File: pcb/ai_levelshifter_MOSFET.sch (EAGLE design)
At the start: 15 parts, among them J1 1X06, J2 1X06NOFIRST, Q1 BSS138, Q2 BSS138, Q3 BSS138, Q4 BSS138

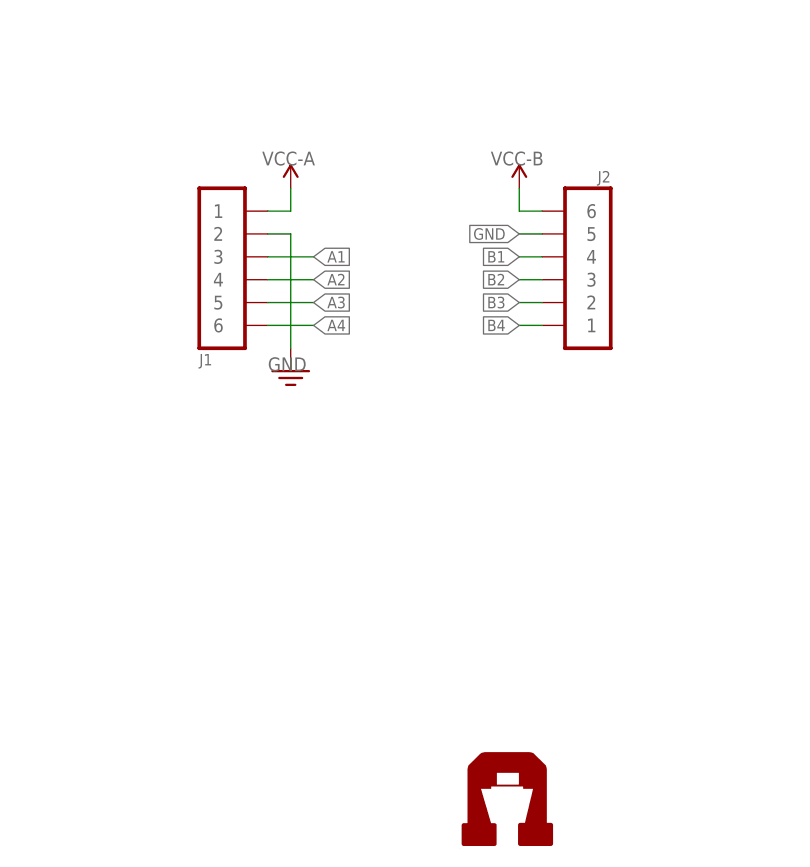
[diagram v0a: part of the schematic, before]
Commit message: fixed spacing to fit properly on a breadboard
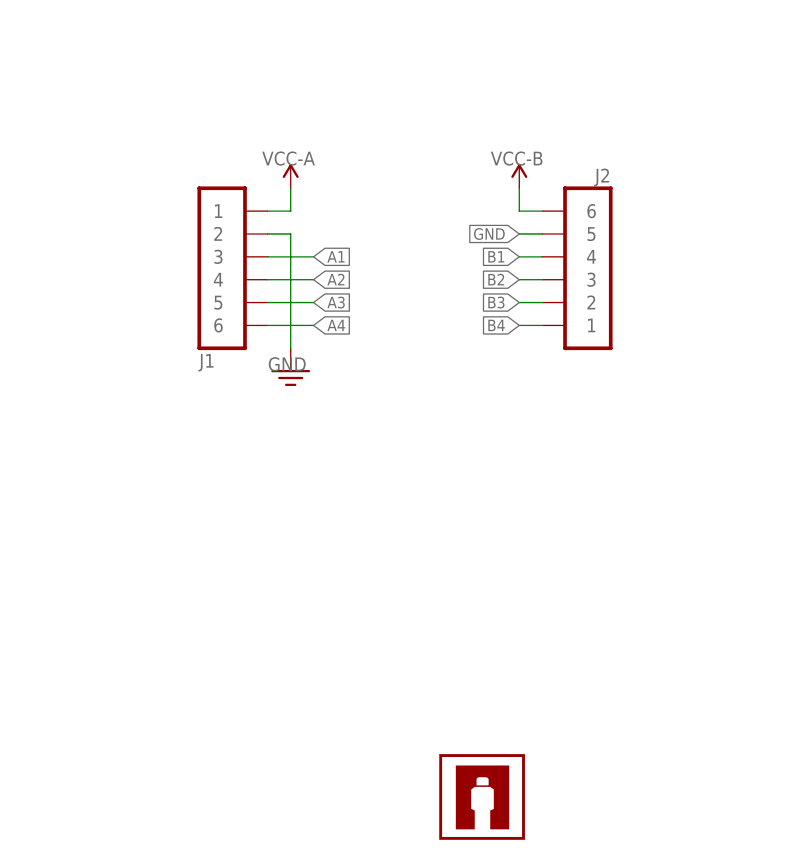
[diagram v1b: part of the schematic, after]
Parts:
- Q1, Q2, Q3, Q4: device Ai_DiscreteSemis:N-FET-BSS138 -> Ai_DiscreteSemis:FET-NMOS-BSS138
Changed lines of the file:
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@@
 <layer number="56" name="wert" color="7" fill="1" visible="no" active="no"/>
 <layer number="57" name="tCAD" color="7" fill="1" visible="no" active="no"/>
+<layer number="90" name="Modules" color="5" fill="1" visible="no" active="no"/>
 <layer number="91" name="Nets" color="2" fill="1" visible="yes" active="yes"/>
 <layer number="92" name="Busses" color="1" fill="1" visible="yes" active="yes"/>
@@
 </classes>
 <parts>
-<part name="Q1" library="Ai_DiscreteSemis" deviceset="N-FET" device="-BSS138" value="BSS138"/>
+<part name="Q1" library="Ai_DiscreteSemis" deviceset="FET-NMOS" device="-BSS138" value="BSS138"/>
 <part name="R1" library="Ai_Passives" deviceset="RES" device="0603" value="10K"/>
 <part name="R2" library="Ai_Passives" deviceset="RES" device="0603" value="10K"/>
-<part name="Q2" library="Ai_DiscreteSemis" deviceset="N-FET" device="-BSS138" value="BSS138"/>
+<part name="Q2" library="Ai_DiscreteSemis" deviceset="FET-NMOS" device="-BSS138" value="BSS138"/>
 <part name="R3" library="Ai_Passives" deviceset="RES" device="0603" value="10K"/>
 <part name="R4" library="Ai_Passives" deviceset="RES" device="0603" value="10K"/>
-<part name="Q3" library="Ai_DiscreteSemis" deviceset="N-FET" device="-BSS138" value="BSS138"/>
+<part name="Q3" library="Ai_DiscreteSemis" deviceset="FET-NMOS" device="-BSS138" value="BSS138"/>
 <part name="R5" library="Ai_Passives" deviceset="RES" device="0603" value="10K"/>
 <part name="R6" library="Ai_Passives" deviceset="RES" device="0603" value="10K"/>
-<part name="Q4" library="Ai_DiscreteSemis" deviceset="N-FET" device="-BSS138" value="BSS138"/>
+<part name="Q4" library="Ai_DiscreteSemis" deviceset="FET-NMOS" device="-BSS138" value="BSS138"/>
 <part name="R7" library="Ai_Passives" deviceset="RES" device="0603" value="10K"/>
 <part name="R8" library="Ai_Passives" deviceset="RES" device="0603" value="10K"/>
@@
 <instance part="FRAME1" gate="G$2" x="147.32" y="0"/>
 <instance part="J1" gate="M06X1" x="109.22" y="76.2" rot="MR180"/>
-<instance part="U$1" gate="G$1" x="140.97" y="17.78"/>
+<instance part="U$1" gate="G$1" x="133.35" y="13.97"/>
 <instance part="U$2" gate="G$1" x="40.64" y="132.08"/>
 <instance part="U$3" gate="G$1" x="93.98" y="132.08"/>
